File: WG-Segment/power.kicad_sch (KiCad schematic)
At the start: 12 parts, among them U301 AP63205WU, U302 MIC5504-3.3YM5, U303 REF3033

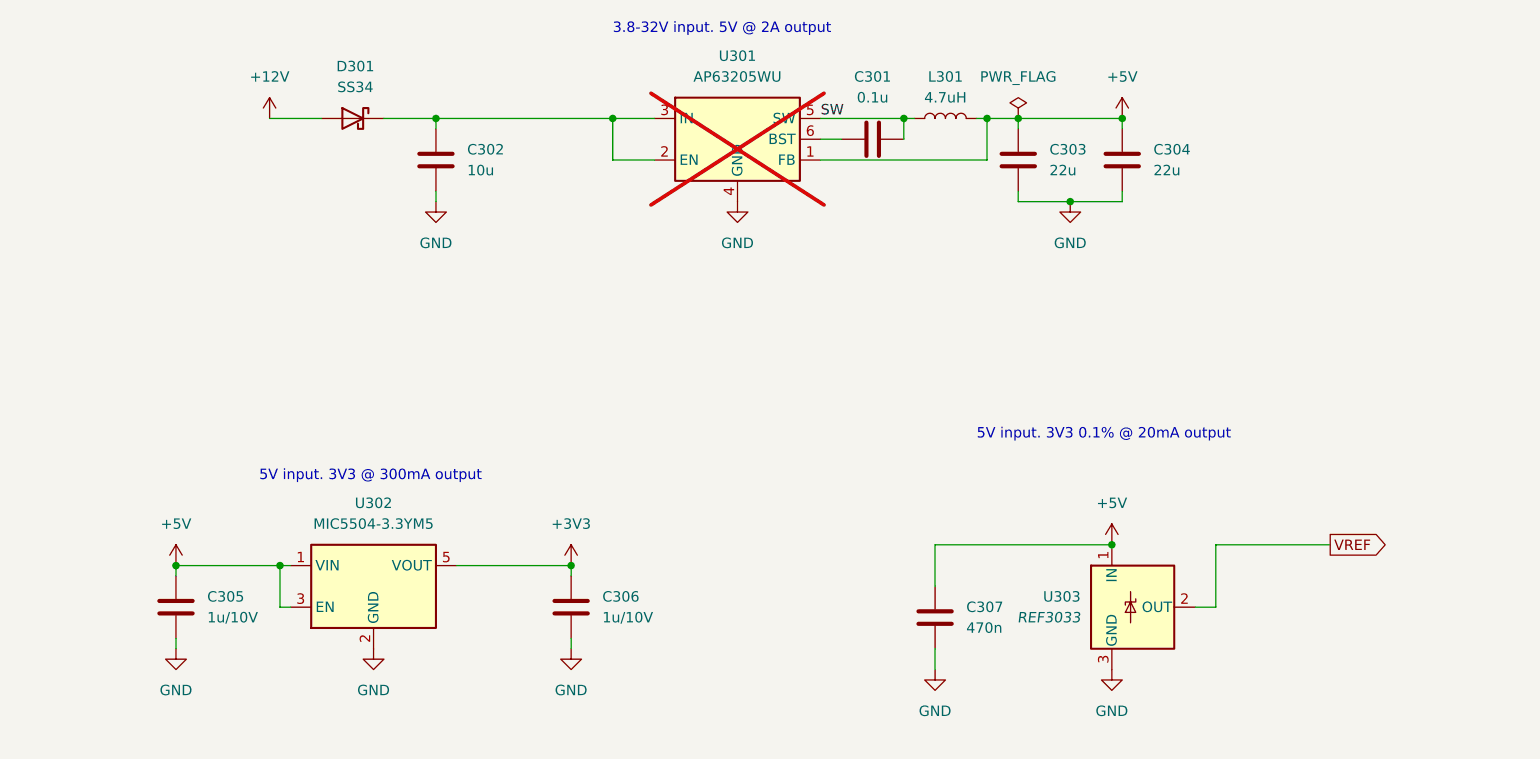
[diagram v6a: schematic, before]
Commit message: Update regulator
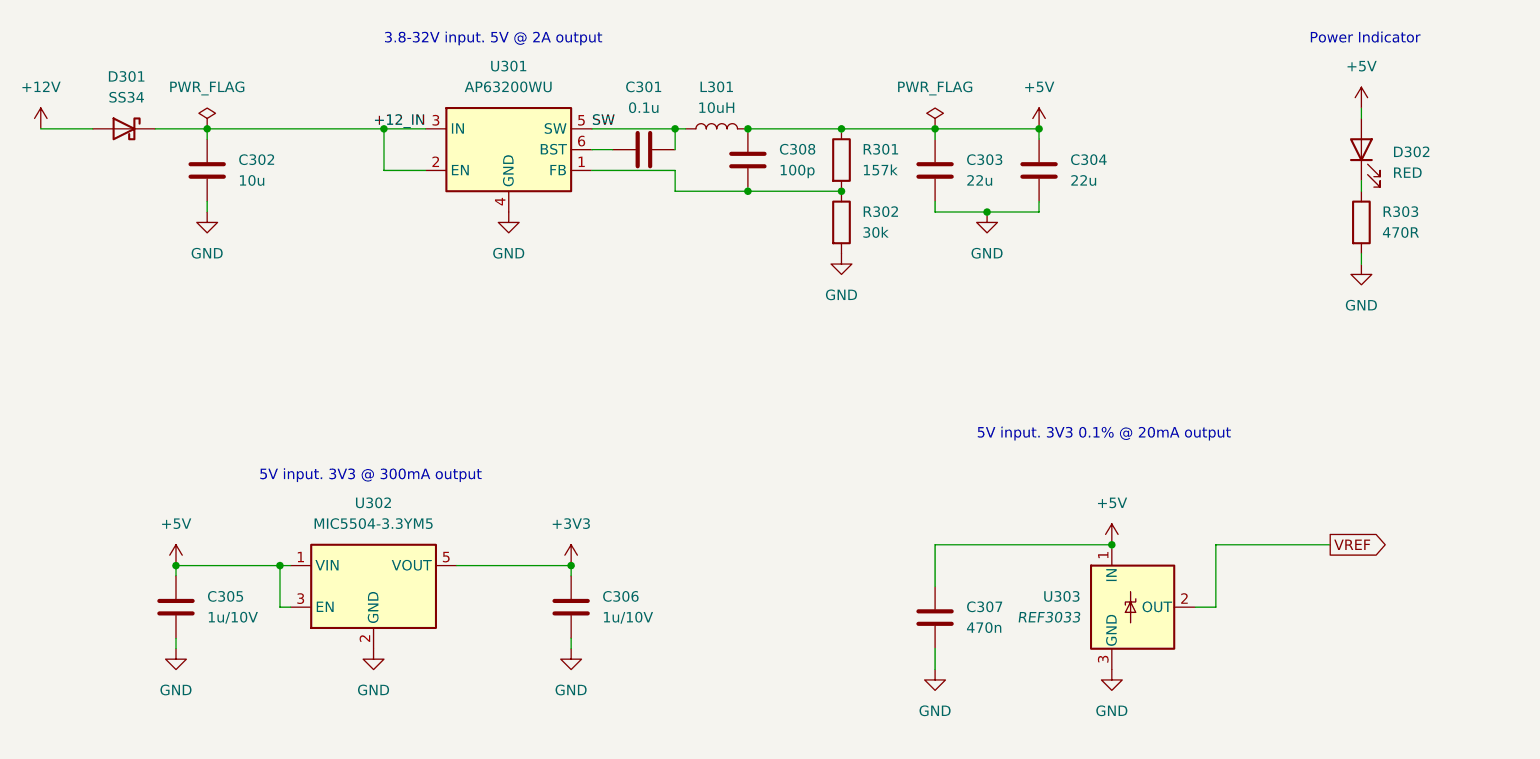
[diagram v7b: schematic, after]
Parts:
- removed U301: AP63205WU, Package_TO_SOT_SMD:TSOT-23-6, symbol Regulator_Switching:AP63205WU
- added C308: 100p, Capacitor_SMD:C_0402_1005Metric_Pad0.74x0.62mm_HandSolder, symbol Device:C
- added D302: RED, LED_SMD:LED_0603_1608Metric_Pad1.05x0.95mm_HandSolder, symbol Device:LED
- added R301: 157k, Resistor_SMD:R_0402_1005Metric_Pad0.72x0.64mm_HandSolder, symbol Device:R
- added R302: 30k, Resistor_SMD:R_0402_1005Metric_Pad0.72x0.64mm_HandSolder, symbol Device:R
- added R303: 470R, Resistor_SMD:R_0402_1005Metric_Pad0.72x0.64mm_HandSolder, symbol Device:R
- added U301: AP63200WU, Package_TO_SOT_SMD:TSOT-23-6, symbol Regulator_Switching:AP63200WU
- L301: value 4.7uH -> 10uH; footprint WordGameLib:Murata_1255AY -> WordGameLib:Murata_6060; Desc IND 4.7uH <100mOhm >2.5A -> IND 10uH <100mOhm Isat>2A; Part Number 1255AY-4R7M=P3 -> 1264EY-100M=P3
- U303: Part Number REF3033 -> REF3033AIDBZR
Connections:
- net +5V: now also C308.1, D302.2 (A), R301.1
- net GND: now also R302.2, R303.2, U301.4 (GND)
- net SW: now also U301.5 (SW)
- net +12_IN: now reaches C302.1, D301.1 (K)
- net +12_IN: now also U301.2 (EN), U301.3 (IN)
- net at C301.1: now also U301.6 (BST)
- new net: D302.1 (K), R303.1
- new net: C308.2, R301.2, R302.1, U301.1 (FB)
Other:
- note added: "Power Indicator"
- moved on the sheet: C301, C302, C303, C304, D301, L301

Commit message: Updates for smoother JLCPCB ordering
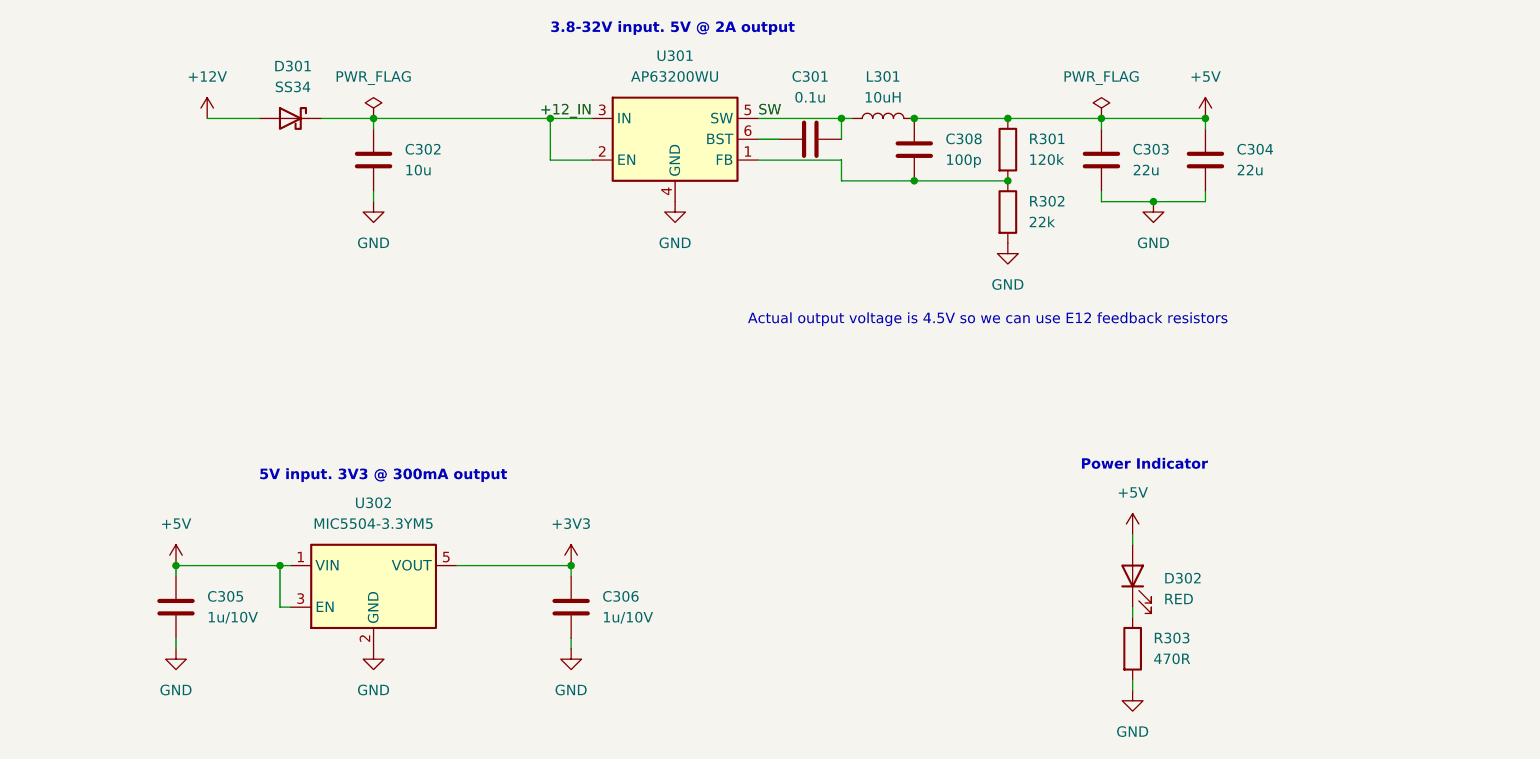
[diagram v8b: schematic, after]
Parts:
- removed C307: 470n, Capacitor_SMD:C_0402_1005Metric_Pad0.74x0.62mm_HandSolder, symbol Device:C
- removed U303: REF3033, Package_TO_SOT_SMD:SOT-23, symbol Reference_Voltage:REF3033
- C308: Desc CAP CER 100p 10V 0805 -> CAP CER 100p 10V 0402
- R301: value 157k -> 120k
- R302: value 30k -> 22k
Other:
- note added: "Actual output voltage is 4.5V so we can use E12 feedback resistors"
- note removed: "5V input. 3V3 0.1% @ 20mA output"
- moved on the sheet: C301, C302, C303, C304, C308, D301, D302, L301, R301, R302, R303, U301
